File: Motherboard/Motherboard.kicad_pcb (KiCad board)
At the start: 4 copper layers, 246.4 x 175.3 mm, 57 parts, among them J1 40-pin IDE Connector, J3 Bus_ISA_8bit, J4 ATX-24, J5 USB_B, J6 ATF15XX_JTAG_ISP, J7 Bus_ISA_8bit, J8 65SIB_Connector, SW1 SW_Push, SW2 SW_SPST, U1 AS6C8008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

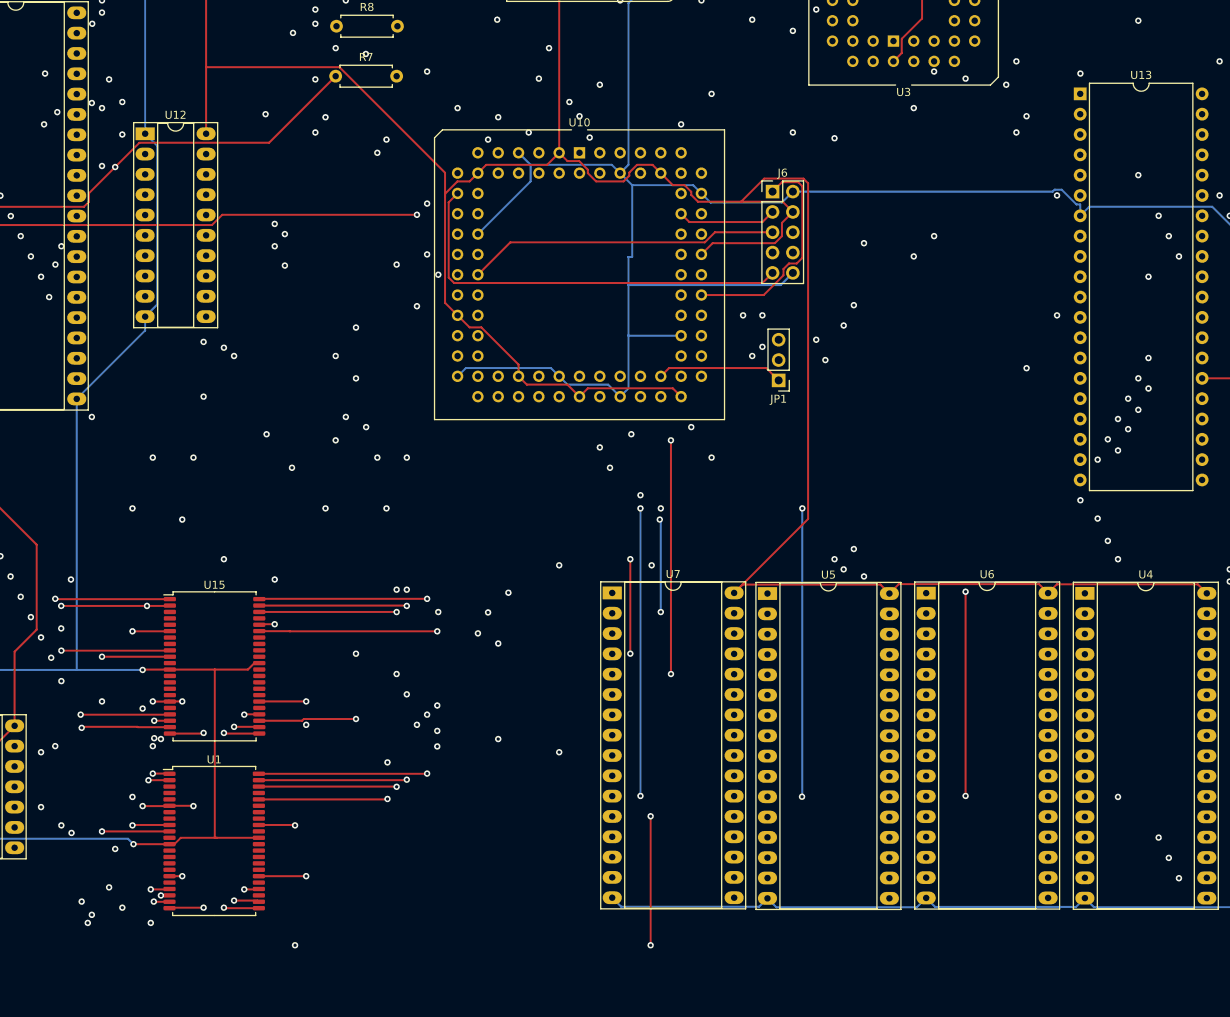
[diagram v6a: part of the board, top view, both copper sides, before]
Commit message: 176 unrouted traces...
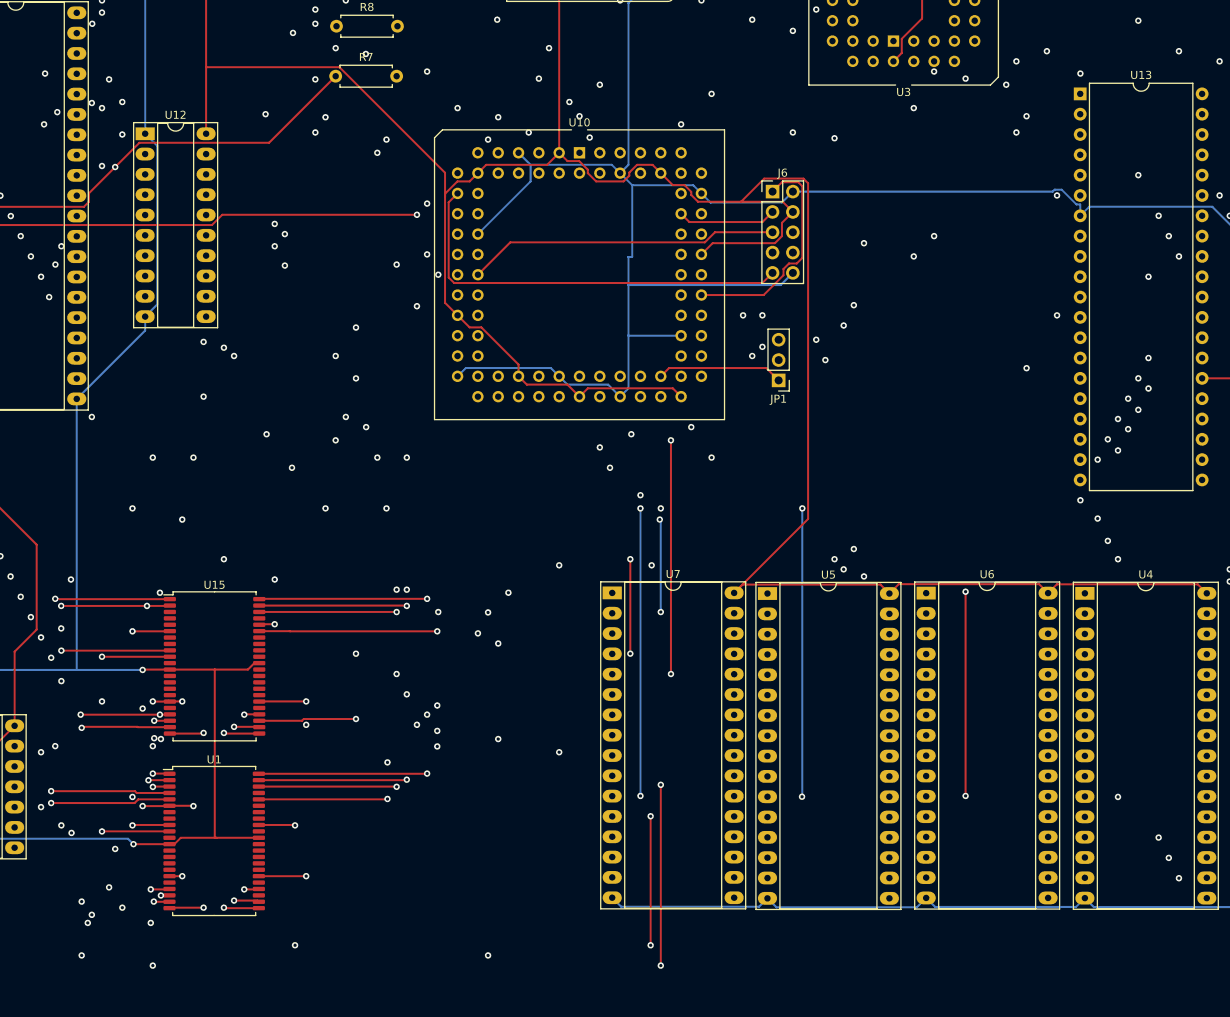
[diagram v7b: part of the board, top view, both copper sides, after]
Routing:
- net A2: track 208.9 -> 320.3 mm, vias 3 -> 7
- net A16: track 151.3 -> 251.8 mm, vias 4 -> 6
- net D2: track 237.0 -> 300.1 mm, vias 7 -> 9
- net A18: track 155.2 -> 214.3 mm, vias 5 -> 7
- net A0: track 323.3 -> 338.3 mm, vias 7 -> 8
- net A1: track 375.3 -> 390.2 mm, vias 11 -> 12

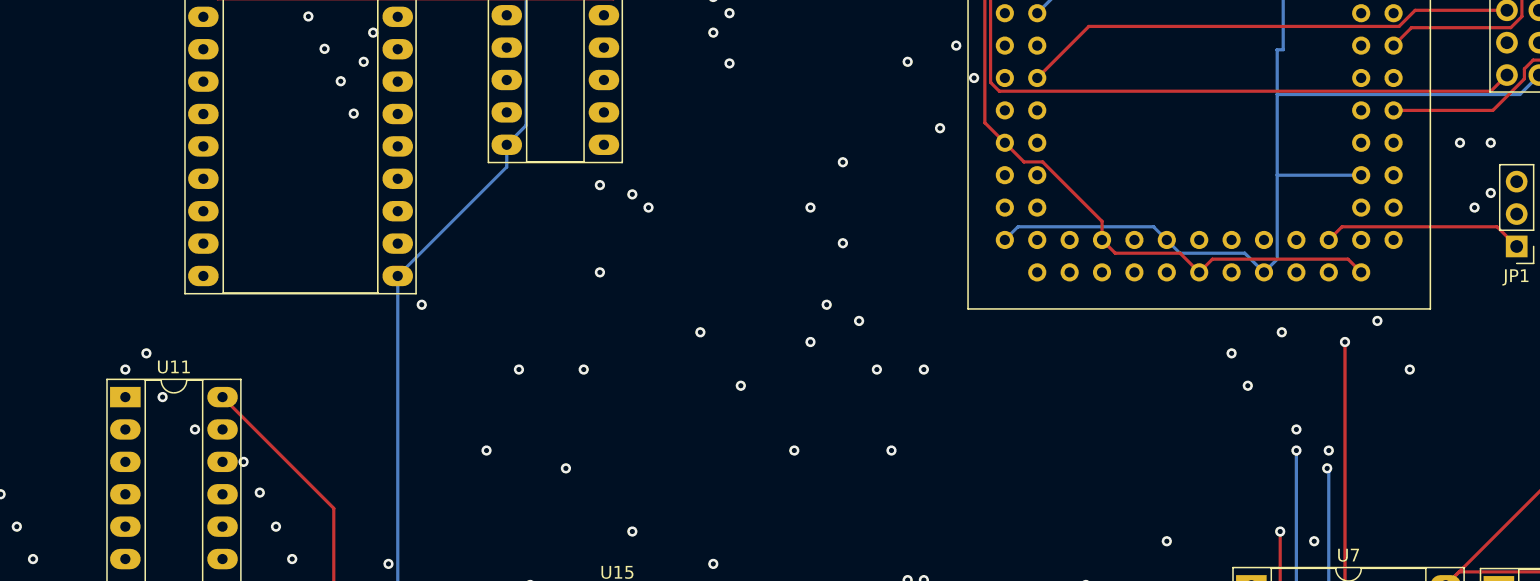
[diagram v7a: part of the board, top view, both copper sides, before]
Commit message: 173 unrouted traces...
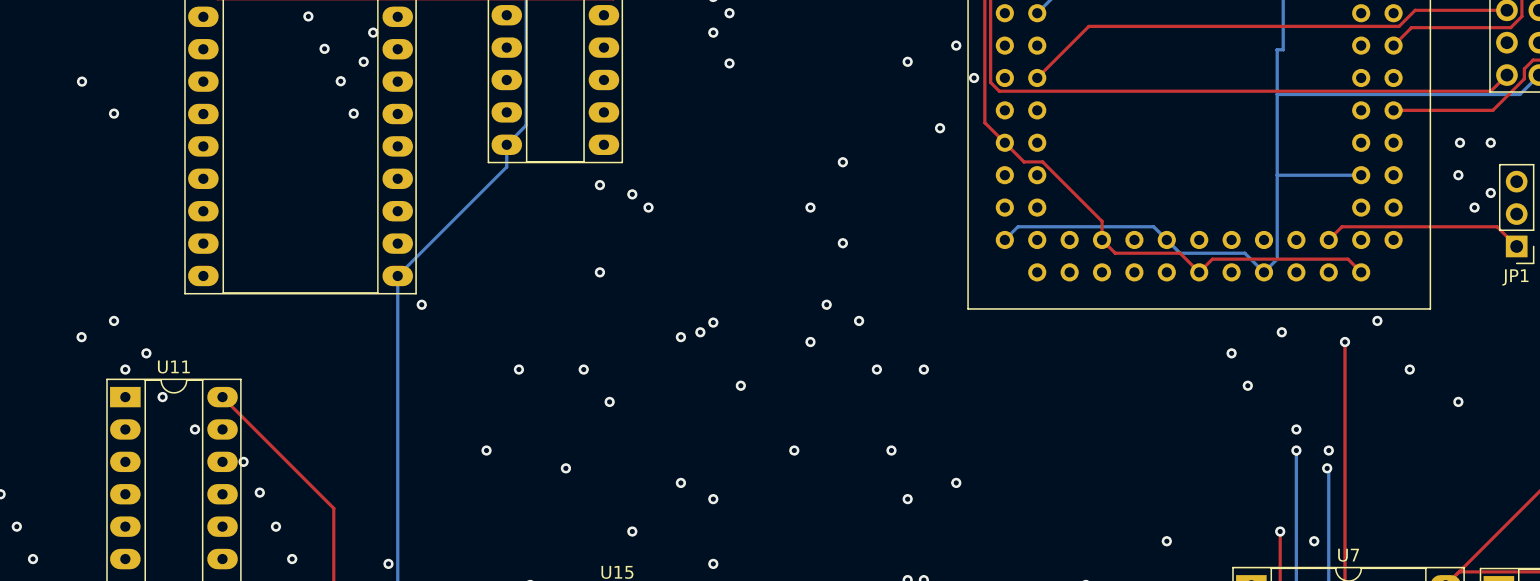
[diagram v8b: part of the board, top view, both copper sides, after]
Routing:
- net ADDR_LOAD: track 0.00 -> 109.8 mm, vias 0 -> 3
- net A5: track 196.0 -> 305.6 mm, vias 4 -> 9
- net A6: track 201.1 -> 300.5 mm, vias 6 -> 11
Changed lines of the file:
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@@
   (via (at 194.31 186.182) (size 0.8) (drill 0.4) (layers "F.Cu" "B.Cu") (net 71))
   (via (at 194.31 184.15) (size 0.8) (drill 0.4) (layers "F.Cu" "B.Cu") (net 71))
+  (via (at 130.81 147.574) (size 0.8) (drill 0.4) (layers "F.Cu" "B.Cu") (net 71))
   (via (at 194.31 197.231) (size 0.8) (drill 0.4) (layers "F.Cu" "B.Cu") (net 71))
   (via (at 193.04 184.15) (size 0.8) (drill 0.4) (layers "F.Cu" "B.Cu") (net 71))
+  (via (at 130.81 163.83) (size 0.8) (drill 0.4) (layers "F.Cu" "B.Cu") (net 71))
+  (via (at 177.8 177.8) (size 0.8) (drill 0.4) (layers "F.Cu" "B.Cu") (net 71))
+  (via (at 193.04 177.8) (size 0.8) (drill 0.4) (layers "F.Cu" "B.Cu") (net 71))
+  (via (at 177.8 163.957) (size 0.8) (drill 0.4) (layers "F.Cu" "B.Cu") (net 71))
   (segment (start 194.31 207.899) (end 194.31 197.231) (width 0.25) (layer "In1.Cu") (net 71))
   (segment (start 258.0566 198.4576) (end 240.52 198.4576) (width 0.25) (layer "In1.Cu") (net 71))
+  (segment (start 130.81 147.574) (end 130.81 163.83) (width 0.25) (layer "In1.Cu") (net 71))
+  (segment (start 193.04 143.51) (end 193.04 177.8) (width 0.25) (layer "In1.Cu") (net 71))
   (segment (start 260.3574 198.4068) (end 259.2324 197.2818) (width 0.25) (layer "In1.Cu") (net 71))
   (segment (start 259.2324 197.2818) (end 258.0566 198.4576) (width 0.25) (layer "In1.Cu") (net 71))
@@
   (segment (start 221.4044 198.6714) (end 219.9894 197.2564) (width 0.25) (layer "In1.Cu") (net 71))
   (segment (start 279.0698 197.3072) (end 277.9702 198.4068) (width 0.25) (layer "In1.Cu") (net 71))
-  (segment (start 193.04 143.51) (end 193.04 184.15) (width 0.25) (layer "In1.Cu") (net 71))
   (segment (start 238.0562 198.6714) (end 221.4044 198.6714) (width 0.25) (layer "In1.Cu") (net 71))
+  (segment (start 177.8 163.957) (end 177.8 177.8) (width 0.25) (layer "In1.Cu") (net 71))
   (segment (start 240.52 198.4576) (end 239.395 197.3326) (width 0.25) (layer "In1.Cu") (net 71))
+  (segment (start 193.04 177.8) (end 193.04 184.15) (width 0.25) (layer "In1.Cu") (net 71))
   (segment (start 239.395 197.3326) (end 238.0562 198.6714) (width 0.25) (layer "In1.Cu") (net 71))
   (segment (start 194.31 184.15) (end 194.31 186.182) (width 0.25) (layer "In1.Cu") (net 71))
+  (segment (start 137.8154 147.6044) (end 130.8404 147.6044) (width 0.25) (layer "In2.Cu") (net 71))
+  (segment (start 130.8404 147.6044) (end 130.81 147.574) (width 0.25) (layer "In2.Cu") (net 71))
+  (segment (start 177.673 163.83) (end 177.8 163.957) (width 0.25) (layer "In2.Cu") (net 71))
   (segment (start 193.04 184.15) (end 194.31 184.15) (width 0.25) (layer "In2.Cu") (net 71))
   (segment (start 203.2 142.24) (end 201.93 143.51) (width 0.25) (layer "In2.Cu") (net 71))
   (segment (start 201.93 143.51) (end 193.04 143.51) (width 0.25) (layer "In2.Cu") (net 71))
+  (segment (start 130.81 163.83) (end 177.673 163.83) (width 0.25) (layer "In2.Cu") (net 71))
   (segment (start 194.3354 197.2564) (end 219.9894 197.2564) (width 0.25) (layer "In2.Cu") (net 71))
+  (segment (start 177.8 177.8) (end 193.04 177.8) (width 0.25) (layer "In2.Cu") (net 71))
   (segment (start 194.31 197.231) (end 194.3354 197.2564) (width 0.25) (layer "In2.Cu") (net 71))
   (segment (start 175.9092 185.293) (end 175.8696 185.3326) (width 0.25) (layer "F.Cu") (net 72))
@@
   (segment (start 196.824 207.163) (end 196.85 207.137) (width 0.25) (layer "F.Cu") (net 72))
   (segment (start 196.85 185.293) (end 175.9092 185.293) (width 0.25) (layer "F.Cu") (net 72))
+  (via (at 175.26 165.1) (size 0.8) (drill 0.4) (layers "F.Cu" "B.Cu") (net 72))
+  (via (at 196.85 176.53) (size 0.8) (drill 0.4) (layers "F.Cu" "B.Cu") (net 72))
   (via (at 196.85 185.293) (size 0.8) (drill 0.4) (layers "F.Cu" "B.Cu") (net 72))
   (via (at 196.85 199.771) (size 0.8) (drill 0.4) (layers "F.Cu" "B.Cu") (net 72))
+  (via (at 175.26 176.53) (size 0.8) (drill 0.4) (layers "F.Cu" "B.Cu") (net 72))
+  (via (at 128.27 165.1) (size 0.8) (drill 0.4) (layers "F.Cu" "B.Cu") (net 72))
   (via (at 196.85 207.137) (size 0.8) (drill 0.4) (layers "F.Cu" "B.Cu") (net 72))
+  (via (at 128.3004 145.0644) (size 0.8) (drill 0.4) (layers "F.Cu" "B.Cu") (net 72))
   (via (at 196.85 142.24) (size 0.8) (drill 0.4) (layers "F.Cu" "B.Cu") (net 72))
   (segment (start 219.9894 199.7964) (end 221.1144 200.9214) (width 0.25) (layer "In1.Cu") (net 72))
+  (segment (start 196.85 176.53) (end 196.85 142.24) (width 0.25) (layer "In1.Cu") (net 72))
+  (segment (start 128.3004 165.0696) (end 128.27 165.1) (width 0.25) (layer "In1.Cu") (net 72))
   (segment (start 240.81 201.2876) (end 257.7666 201.2876) (width 0.25) (layer "In1.Cu") (net 72))
   (segment (start 196.85 207.137) (end 196.85 199.771) (width 0.25) (layer "In1.Cu") (net 72))
+  (segment (start 175.26 165.1) (end 175.26 176.53) (width 0.25) (layer "In1.Cu") (net 72))
   (segment (start 257.7666 201.2876) (end 259.2324 199.8218) (width 0.25) (layer "In1.Cu") (net 72))
   (segment (start 239.395 199.8726) (end 240.81 201.2876) (width 0.25) (layer "In1.Cu") (net 72))
@@
   (segment (start 260.4082 200.9976) (end 277.9194 200.9976) (width 0.25) (layer "In1.Cu") (net 72))
   (segment (start 277.9194 200.9976) (end 279.0698 199.8472) (width 0.25) (layer "In1.Cu") (net 72))
+  (segment (start 128.3004 145.0644) (end 128.3004 165.0696) (width 0.25) (layer "In1.Cu") (net 72))
   (segment (start 221.1144 200.9214) (end 238.3462 200.9214) (width 0.25) (layer "In1.Cu") (net 72))
+  (segment (start 196.85 185.293) (end 196.85 176.53) (width 0.25) (layer "In1.Cu") (net 72))
   (segment (start 259.2324 199.8218) (end 260.4082 200.9976) (width 0.25) (layer "In1.Cu") (net 72))
   (segment (start 238.3462 200.9214) (end 239.395 199.8726) (width 0.25) (layer "In1.Cu") (net 72))
-  (segment (start 196.85 185.293) (end 196.85 142.24) (width 0.25) (layer "In1.Cu") (net 72))
+  (segment (start 175.26 176.53) (end 196.85 176.53) (width 0.25) (layer "In2.Cu") (net 72))
+  (segment (start 175.26 165.1) (end 128.27 165.1) (width 0.25) (layer "In2.Cu") (net 72))
   (segment (start 196.8754 199.7964) (end 196.85 199.771) (width 0.25) (layer "In2.Cu") (net 72))
   (segment (start 196.85 142.24) (end 200.66 142.24) (width 0.25) (layer "In2.Cu") (net 72))
+  (segment (start 128.27 145.034) (end 128.3004 145.0644) (width 0.25) (layer "In2.Cu") (net 72))
   (segment (start 219.9894 199.7964) (end 196.8754 199.7964) (width 0.25) (layer "In2.Cu") (net 72))
+  (segment (start 137.8154 145.0644) (end 128.3004 145.0644) (width 0.25) (layer "In2.Cu") (net 72))
   (segment (start 164.6946 185.3326) (end 150.4076 185.3326) (width 0.25) (layer "F.Cu") (net 73))
   (segment (start 162.56 207.137) (end 164.6178 207.137) (width 0.25) (layer "F.Cu") (net 73))
@@
   (segment (start 250.063 110.49) (end 250.063 109.22) (width 0.25) (layer "In2.Cu") (net 223))
   (segment (start 312.547 219.583) (end 320.167 219.583) (width 0.25) (layer "In2.Cu") (net 224))
+  (via (at 236.22 170.18) (size 0.8) (drill 0.4) (layers "F.Cu" "B.Cu") (net 225))
+  (via (at 236.22 152.4) (size 0.8) (drill 0.4) (layers "F.Cu" "B.Cu") (net 225))
+  (via (at 169.672 170.18) (size 0.8) (drill 0.4) (layers "F.Cu" "B.Cu") (net 225))
+  (segment (start 169.672 170.18) (end 169.672 150.4646) (width 0.25) (layer "In1.Cu") (net 225))
+  (segment (start 236.22 152.4) (end 236.22 170.18) (width 0.25) (layer "In1.Cu") (net 225))
+  (segment (start 169.672 150.4646) (end 169.2248 150.0174) (width 0.25) (layer "In1.Cu") (net 225))
+  (segment (start 231.14 152.4) (end 236.22 152.4) (width 0.25) (layer "In2.Cu") (net 225))
+  (segment (start 169.672 170.18) (end 236.22 170.18) (width 0.25) (layer "In2.Cu") (net 225))
   (via (at 278.511 119.634) (size 0.8) (drill 0.4) (layers "F.Cu" "B.Cu") (net 226))
   (segment (start 278.511 119.634) (end 278.4856 119.6594) (width 0.25) (layer "In1.Cu") (net 226))
